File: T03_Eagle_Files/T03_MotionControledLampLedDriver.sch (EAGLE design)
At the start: 30 parts, among them U1 ATMEGA328P-MU, U4 TPS61161ADRVT, X2 16MHz

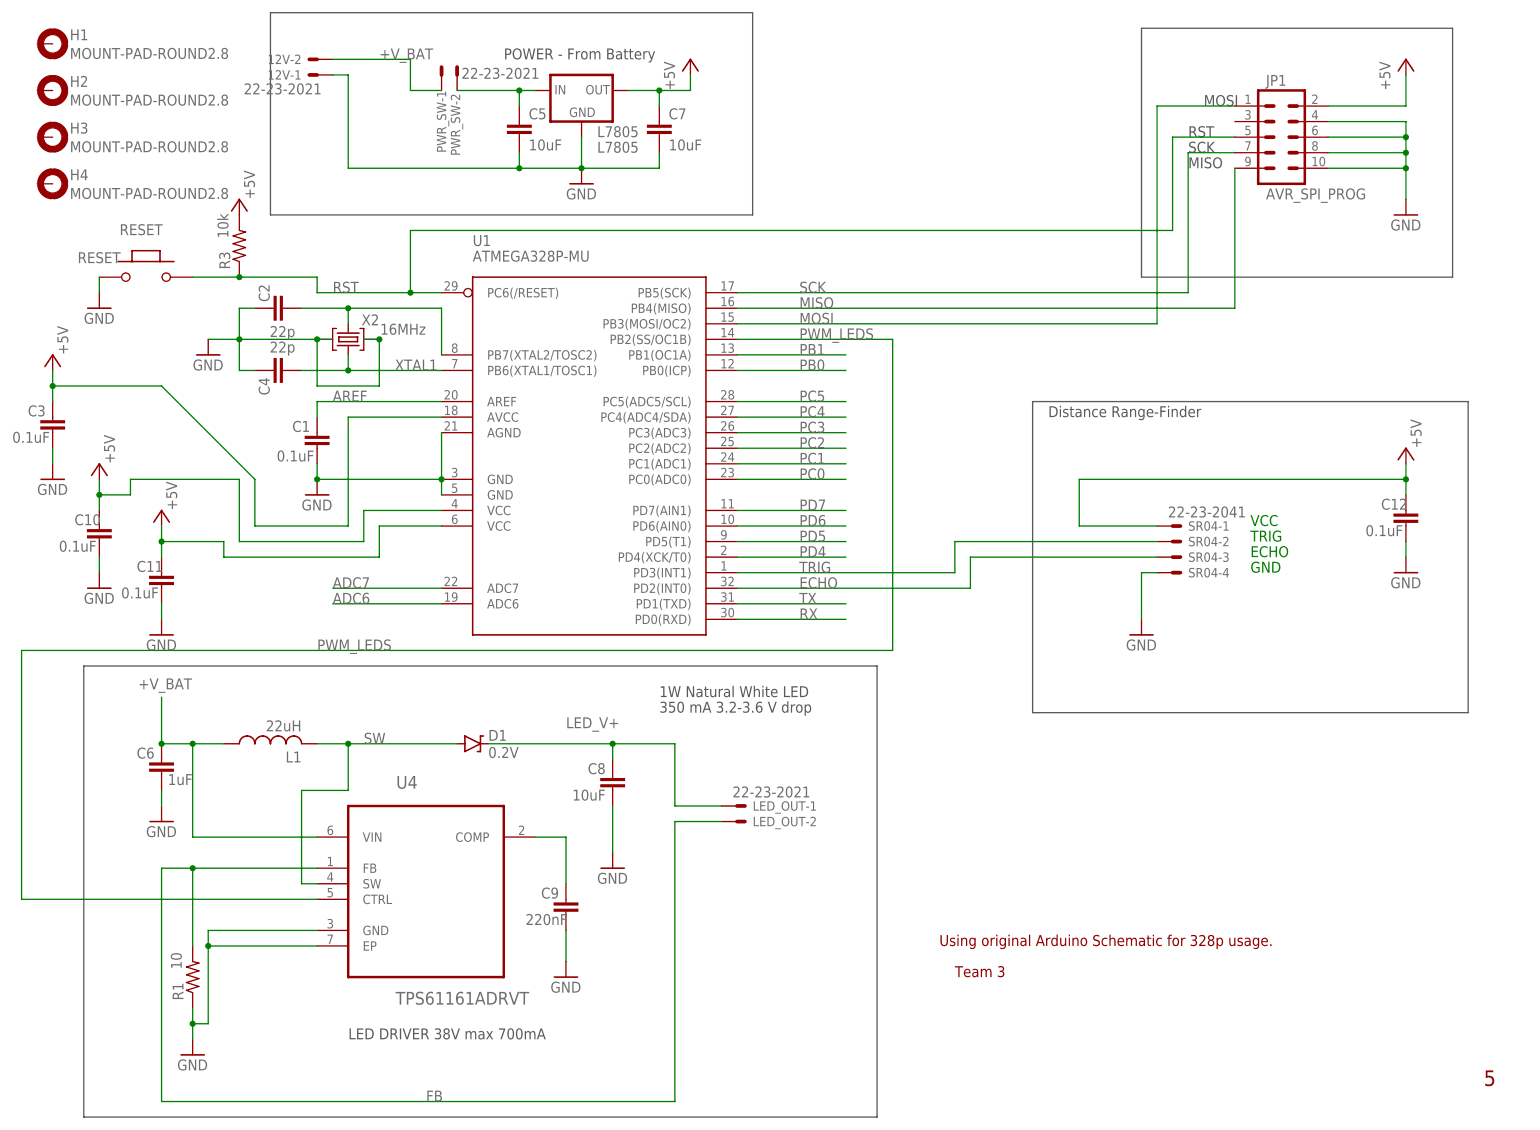
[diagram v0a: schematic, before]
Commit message: Board Layouts finished, ready for OSH
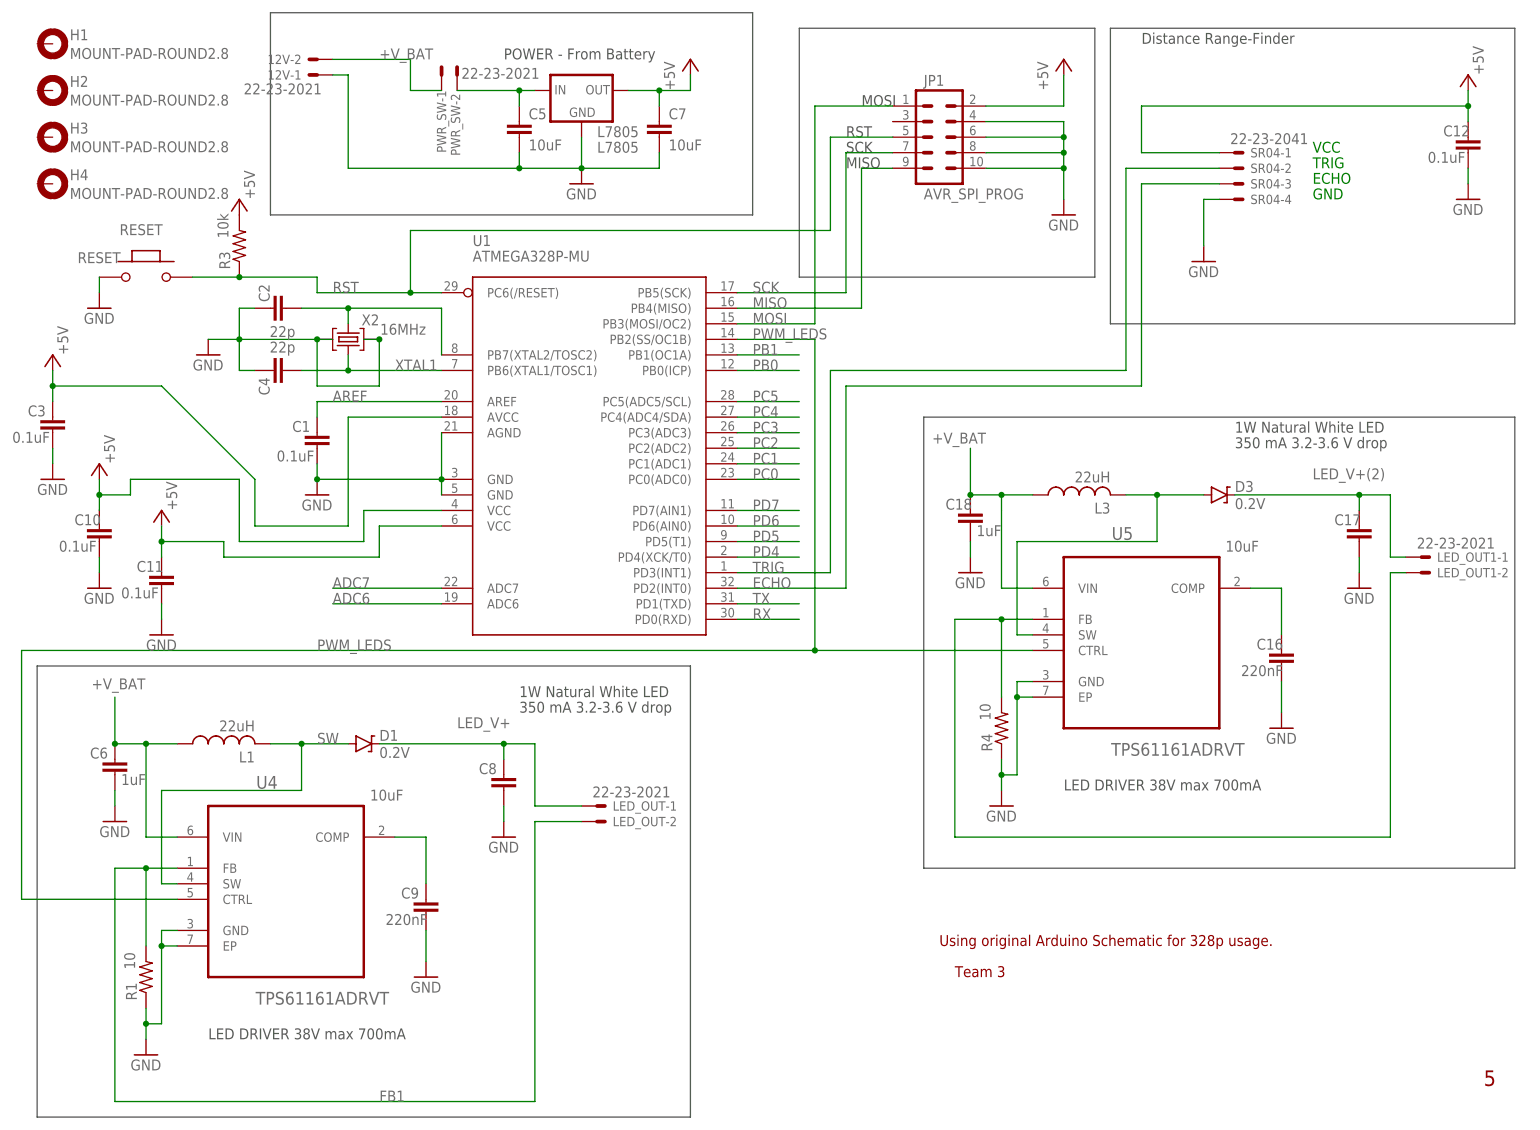
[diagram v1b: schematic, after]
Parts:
- added C16: 220nF, Smartprj:C-EUC0603
- added C17: 10uF, Smartprj:C-EUC0603
- added C18: 1uF, Smartprj:C-EUC0603
- added D3: 0.2V, SparkFun-DiscreteSemi:DIODE-ZENER3.3V
- added L3: 22uH, rcl:L-USL4532P
- added LED_OUT1: 22-23-2021, con-molex:22-23-2021
- added R4: 10, rcl:R-US_M1206
- added U5: TPS61161ADRVT, Texas Instruments_By_element14_Batch_1:TPS61161ADRVT
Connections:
- net FB renamed FB1
- new net COMP1: C16.2, U5.COMP
- new net FB2: LED_OUT1-2.S, R4.2, U5.FB
- new net LED_V+(2): C17.2, D3.C, LED_OUT1-1.S
- new net SW1: D3.A, L3.2, U5.SW
- net +V_BAT: now also C18.2, L3.1, U5.VIN
- net GND: now also C16.1, C17.1, C18.1, R4.1, U5.EP, U5.GND
- net PWM_LEDS: now also U5.CTRL
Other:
- moved on the sheet: C12, C6, C8, C9, D1, JP1, L1, LED_OUT-1, LED_OUT-2, R1, SR04-1, SR04-2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
